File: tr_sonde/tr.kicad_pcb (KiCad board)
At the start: 4 copper layers, 108.2 x 67.3 mm, 93 parts, among them J1 SMA, J2 SMA, J3 SMA, K1 TR, K2 HV_MON, K3 VINHDR, K4 TR, Q1 PBSS4250X, Q2 MMBT2222A, Q3 STD2NK90ZT4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

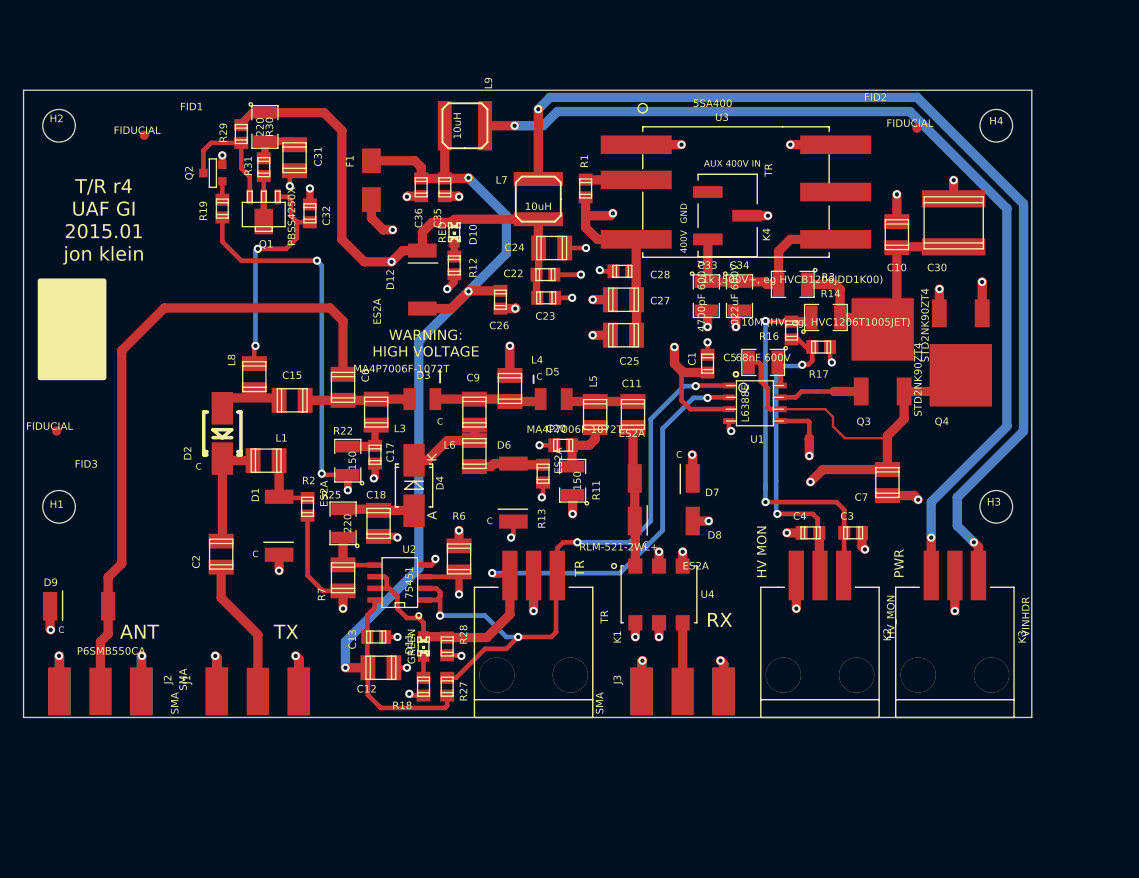
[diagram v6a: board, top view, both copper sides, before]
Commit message: cleaned up silkscreen, moved fiduciary marks at least 4.75ish mm away from board edges
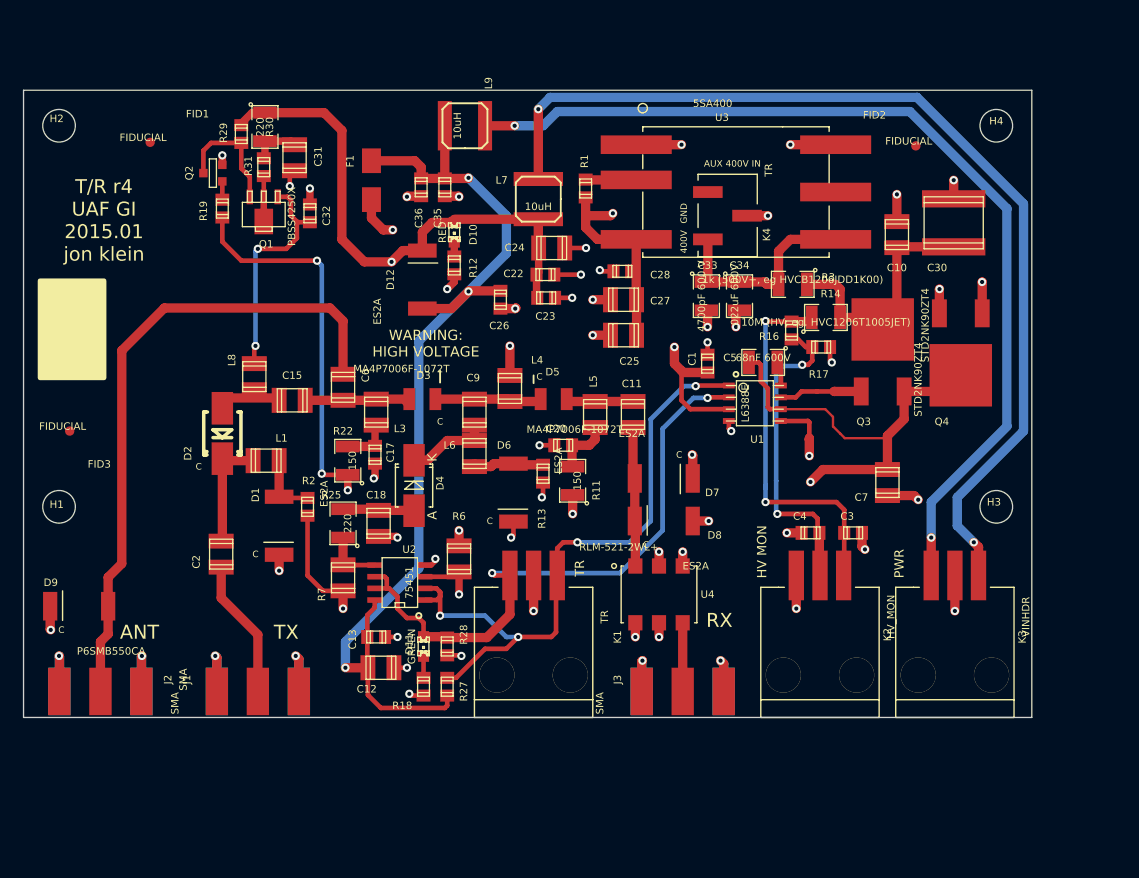
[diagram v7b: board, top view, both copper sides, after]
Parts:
- moved FID2 1.91 mm to (152.1, 30.1)
- moved FID3 1.40 mm to (61.3, 60.7)
- moved FID1 0.99 mm to (70.0, 29.7)

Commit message: DFM changes..
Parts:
- removed C22, C36: 2.2uF, smd_capacitors:c_0805
- removed K4: TR, sdtransmitter:0740991003
- C11, C7, C9: value .022uF, 600 V -> .022uF 600V
- C15, C2, C6: value .022uF 600 V -> .022uF 600V
- C18: value .022uF 100V -> .022uF 600V
- C28: value 100pF -> 10nF
- C33: value 4700pF 600 V -> 4700pF 600V
- D11: value GREEN -> RED
- K1: value TR -> SMDHDR
- K2: value HV_MON -> SMDHDR
- K3: value VINHDR -> SMDHDR
- moved R3 0.99 mm to (139.7, 44.3), turned to 0 degrees
- moved FID3 0.97 mm to (62.2, 60.3)
- moved L6 0.63 mm to (104.8, 63.8)
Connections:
- R3 pad 1: VDD -> Net-(C33-Pad1)
- R3 pad 2: Net-(C33-Pad1) -> VDD
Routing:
- net GND: track 142.6 -> 136.4 mm, vias 53 -> 50
- net Net-(C33-Pad1): track 22.9 -> 17.9 mm
